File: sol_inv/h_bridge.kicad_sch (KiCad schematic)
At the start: 31 parts, among them J1 Screw_Terminal_01x02, J2 Screw_Terminal_01x02, T1 12uH, 1.7A, T2 12uH, 1.7A, T3 12uH, 1.7A, U1 MCP6001-OT, U2 MCP6001-OT, U3 INA240A1D, U4 INA240A1D, U5 IFX007T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

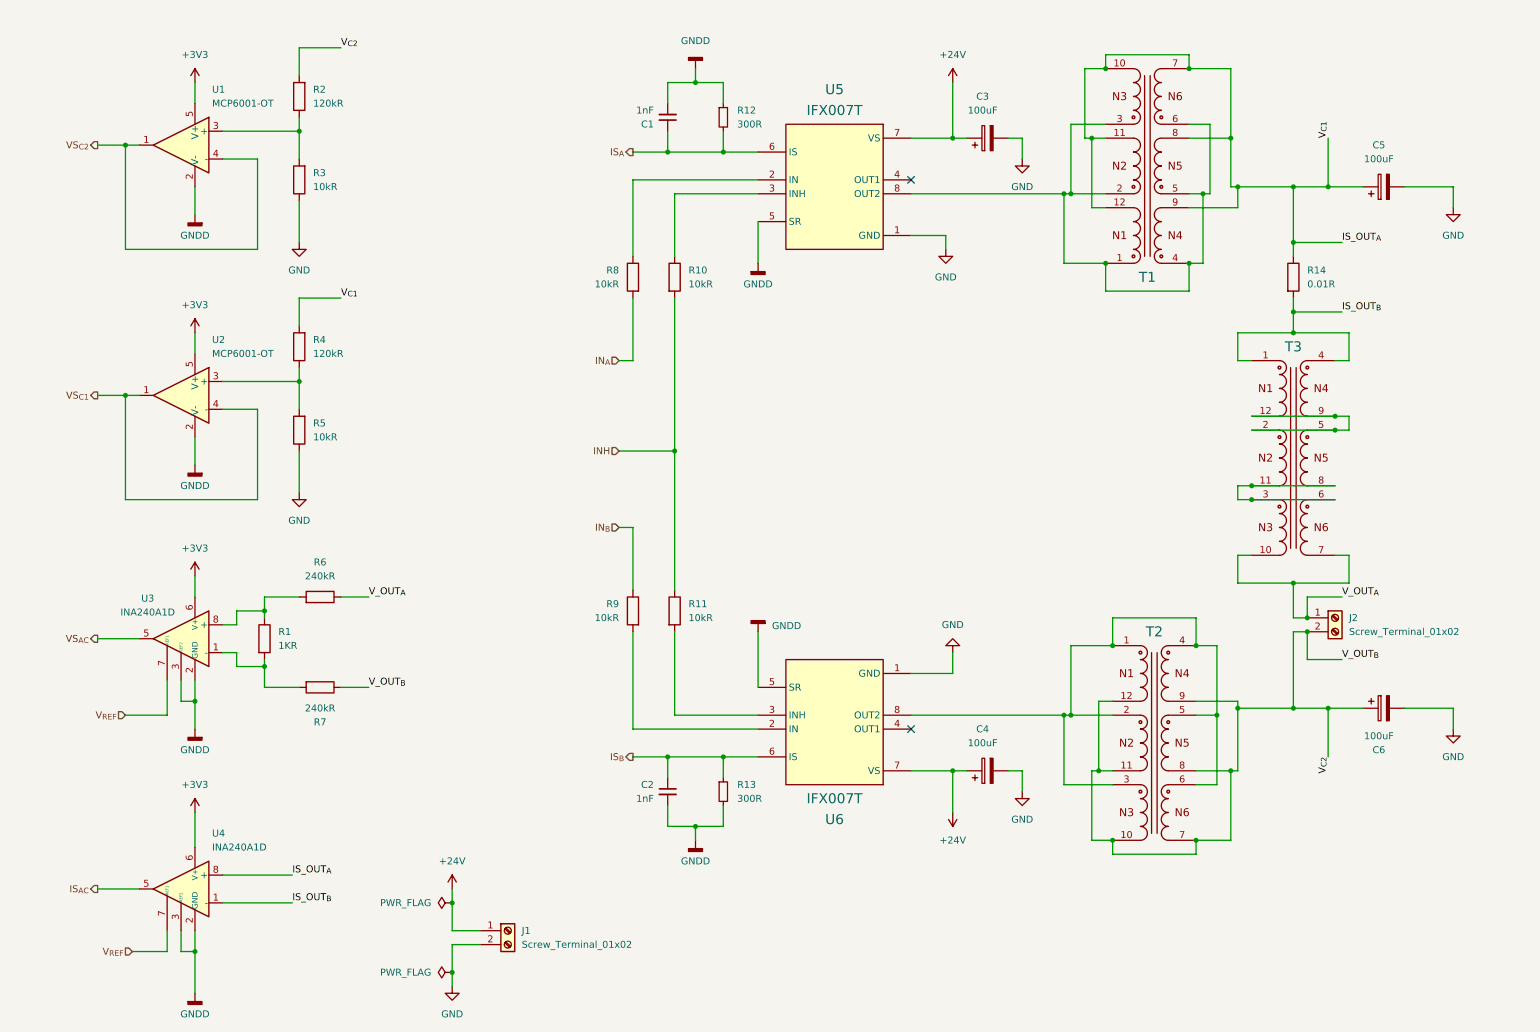
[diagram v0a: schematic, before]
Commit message: v0.2 components change + reference to providers
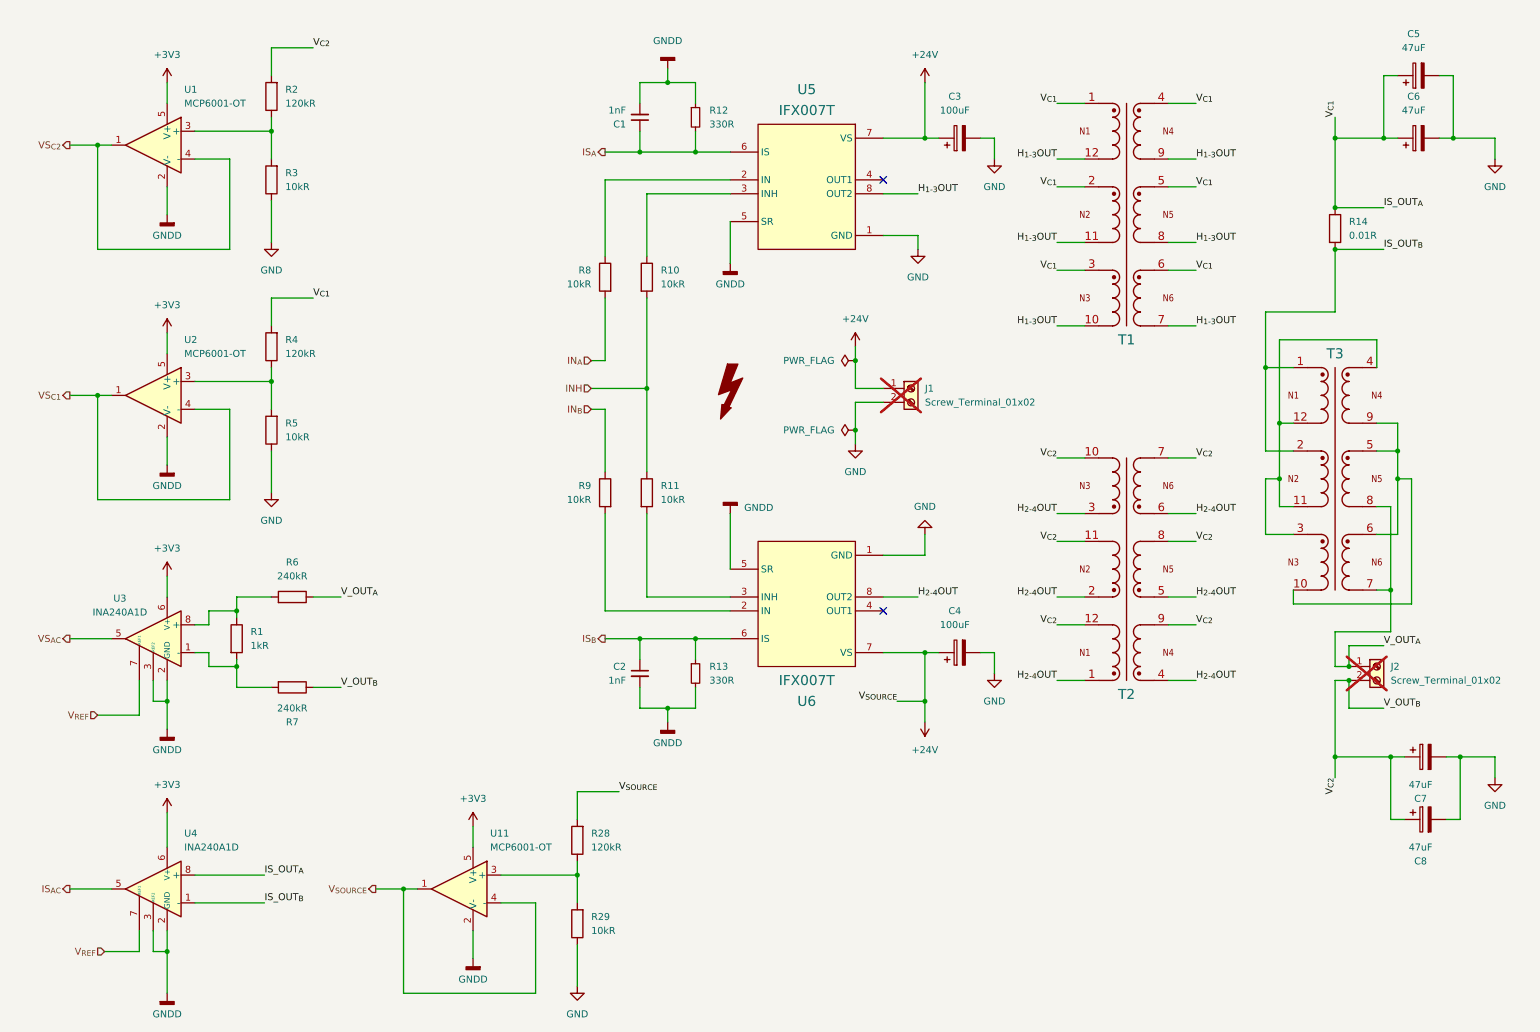
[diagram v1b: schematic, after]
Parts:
- removed C6: 100uF, Capacitor_SMD:CP_Elec_8x10, symbol Device:C_Polarized
- removed T3: 12uH, 1.7A, Eagle_WE-FLEX (rev24a):WE-FLEX_EFD20, symbol WE-FLEX (rev24a):749196521
- added C5, C7, C8: 47uF, Capacitor_SMD:CP_Elec_8x10, symbol Device:C_Polarized
- added R28: 120kR, Resistor_SMD:R_0805_2012Metric, symbol Device:R
- added R29: 10kR, Resistor_SMD:R_2512_6332Metric, symbol Device:R
- added T3: 12uH, 1.7A, Eagle_WE-FLEX (rev24a):WE-FLEX_EFD20, symbol Eagle_WE-FLEX (rev24a):WE-FLEX_EFD20
- added U11: MCP6001-OT, Package_TO_SOT_SMD:SOT-23-5, symbol Amplifier_Operational:MCP6001-OT
- C1, C2: ComponentLink2URL (none) -> https://ro.farnell.com/kemet/c0603c102k5recauto/cap-1000pf-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
- C3, C4: ComponentLink2URL (none) -> https://ro.farnell.com/nichicon/uud1h101mnl1gs/cap-100-f-50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
- C6: renamed from C5; value 100uF -> 47uF; ComponentLink2URL (none) -> https://ro.farnell.com/kemet/a785kn476m1jlas045/cap-alu-ele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
- J1, J2: footprint Wurth-691216610002:691216610002 -> Wurth-WR-TBL Series:691216610002_Handsolder; ComponentLink2URL (none) -> https://ro.farnell.com/wurth-elektronik/691216610002/tb-wir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; now not fitted; now left out of the parts list
- R1: value 1KR -> 1kR; ComponentLink2URL (none) -> https://ro.farnell.com/multicomp-pro/mcmr08x1001ftl/res-1k-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
- R10, R11, R3, R5, R8, R9: ComponentLink2URL (none) -> https://ro.farnell.com/vishay/crcw251210k0fkeg/res-10k-1-1w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
- R12, R13: value 300R -> 330R; footprint Resistor_SMD:R_0402_1005Metric -> Resistor_SMD:R_0603_1608Metric; ComponentLink2URL (none) -> https://ro.farnell.com/te-connectivity/crgcq0603j330r/res-3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
- R14: ComponentLink2URL (none) -> https://ro.farnell.com/te-connectivity/crgcq0603j330r/res-3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
- R2, R4: ComponentLink2URL (none) -> https://ro.farnell.com/panasonic/erjhp6j124v/res-120k-5-0-5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
- R6, R7: ComponentLink2URL (none) -> https://ro.farnell.com/panasonic/erj3red2403v/res-240k-0-5-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
- T1, T2: symbol WE-FLEX (rev24a):749196521 -> Eagle_WE-FLEX (rev24a):WE-FLEX_EFD20; ComponentLink1URL https://www.we-online.com/redexpert/article/749196521?ad -> (none); ComponentLink2URL https://www.we-online.com/redexpert/spec/749196521?ad -> https://ro.mouser.com/ProductDetail/Wurth-Elektronik/749196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
- U1, U2: ComponentLink2URL (none) -> https://ro.mouser.com/ProductDetail/Microchip-Technology/MC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
- U3, U4: ComponentLink2URL (none) -> https://ro.mouser.com/ProductDetail/Texas-Instruments/INA24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
- U5, U6: ComponentLink2URL (none) -> https://ro.mouser.com/ProductDetail/Infineon-Technologies/I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
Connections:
- net +24V: now also R28.2, U11.1, U11.4 (-)
- net +3V3: now also U11.5 (V+)
- net GND: now also C5.2, C7.2, C8.2, R29.1
- net GNDD: now also U11.2 (V-)
- net IS_OUT_{A}: now also T1.1, T1.2, T1.3, T1.4, T1.5, T1.6, C5.1; no longer T1.10, T1.11, T1.12, T1.7, T1.8, T1.9
- net IS_OUT_{B}: now also T3.1, T3.2
- net V_OUT_{A}: now also T3.7, T3.8
- net V_OUT_{B}: now also C7.1, C8.1
- net H_{2-4}OUT: now reaches T2.1, T2.2, T2.3, T2.4, T2.5, T2.6, U6.8 (OUT2)
- new net: R28.1, R29.2, U11.3 (+)
- new net: T3.10, T3.5, T3.6, T3.9
- new net: T3.11, T3.12, T3.3, T3.4
- new net H_{1-3}OUT: T1.10, T1.11, T1.12, T1.7, T1.8, T1.9, U5.8 (OUT2)
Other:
- moved on the sheet: C1, C2, C3, C4, C6, R1, R10, R11, R12, R13, R14, R2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

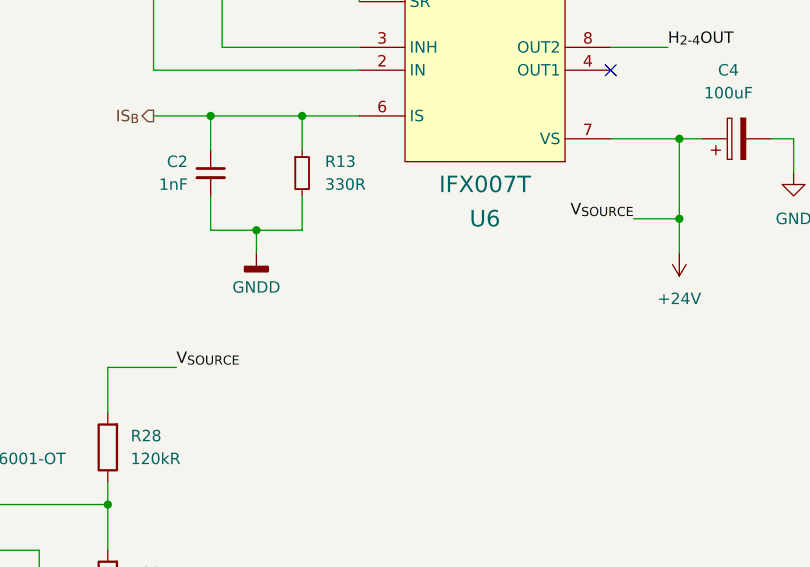
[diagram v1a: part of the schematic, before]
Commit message: initial component placement
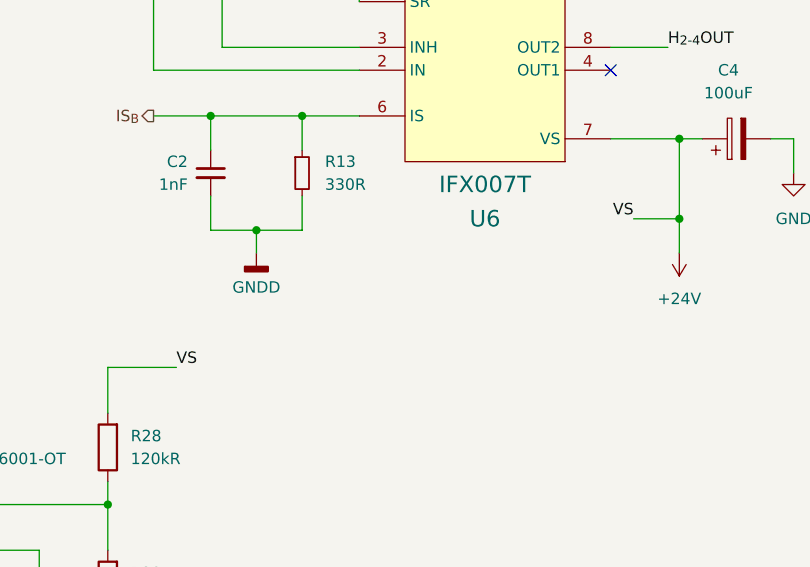
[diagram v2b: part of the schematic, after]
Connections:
- net +24V: no longer U11.1, U11.4 (-)
- new net V_{SOURCE}: U11.1, U11.4 (-)
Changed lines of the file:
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@@
 	(title_block
 		(title "H-Bridge Current Conversion")
-		(date "2025-04-10")
-		(rev "0.2")
+		(date "2025-04-24")
+		(rev "0.2.1")
 		(company "Cezar-Octavian Bontaș")
 	)
@@
 		)
 	)
-	(label "V_{SOURCE}"
+	(label "VS"
 		(at 171.45 135.89 180)
 		(effects
@@
 		)
 	)
-	(label "V_{SOURCE}"
+	(label "VS"
 		(at 120.65 152.4 0)
 		(effects
@@
 		(at 140.97 78.74 0)
 		(unit 1)
-		(exclude_from_sim yes)
+		(exclude_from_sim no)
 		(in_bom no)
 		(on_board no)

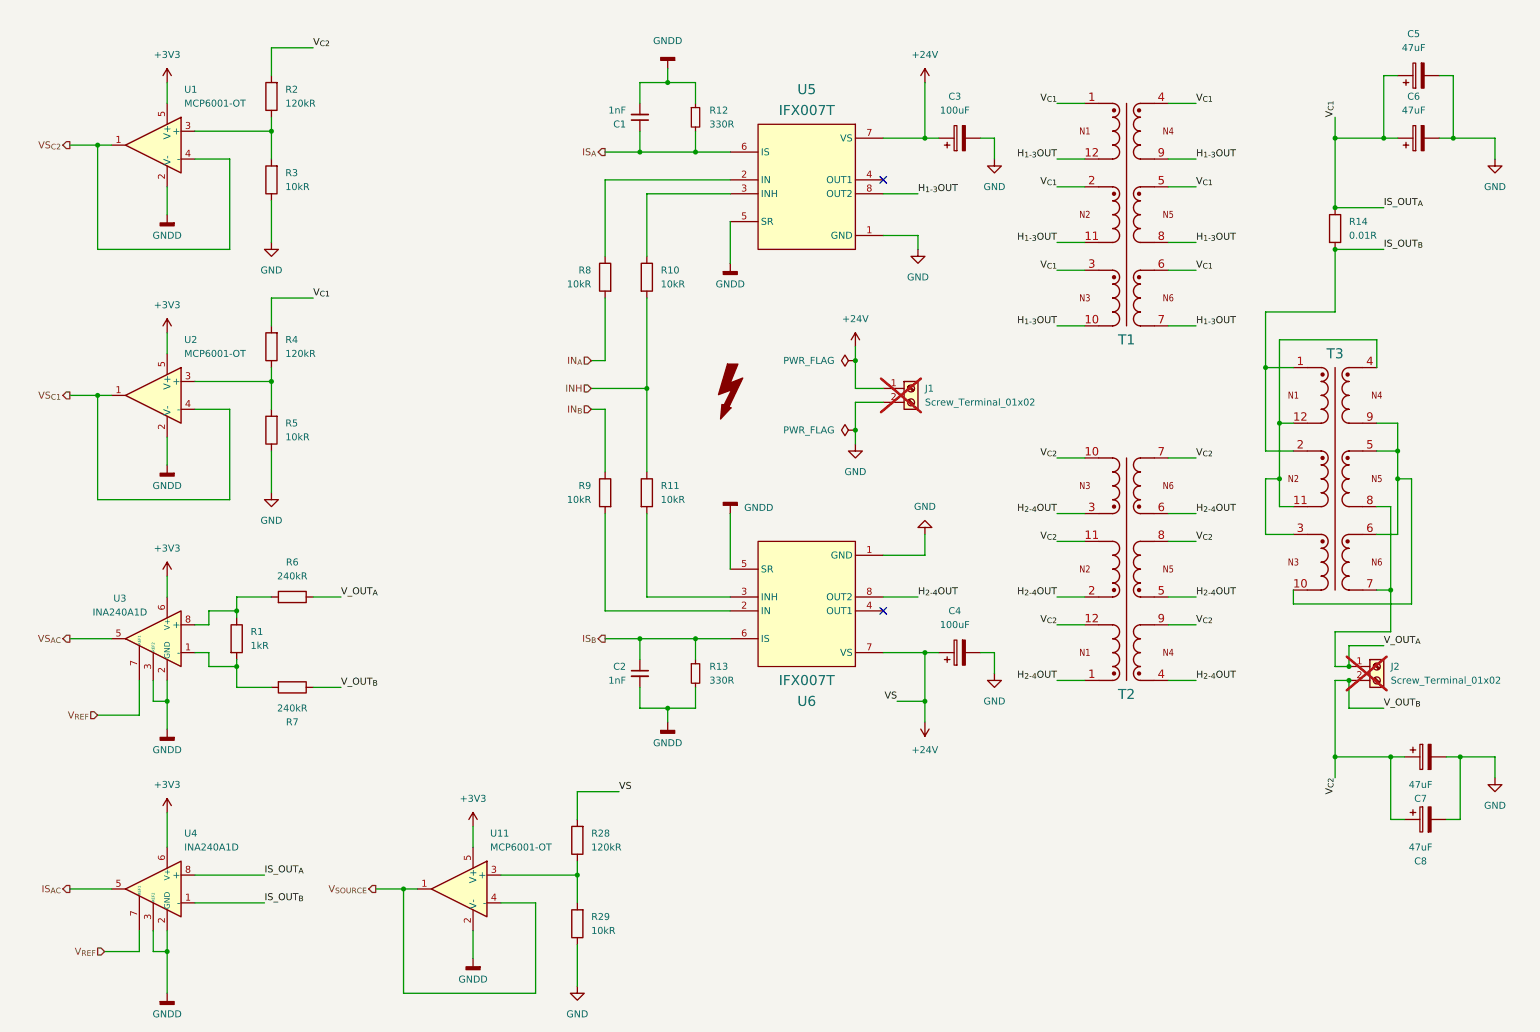
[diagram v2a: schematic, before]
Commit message: v0.3 pcb layout pre-drc fixes
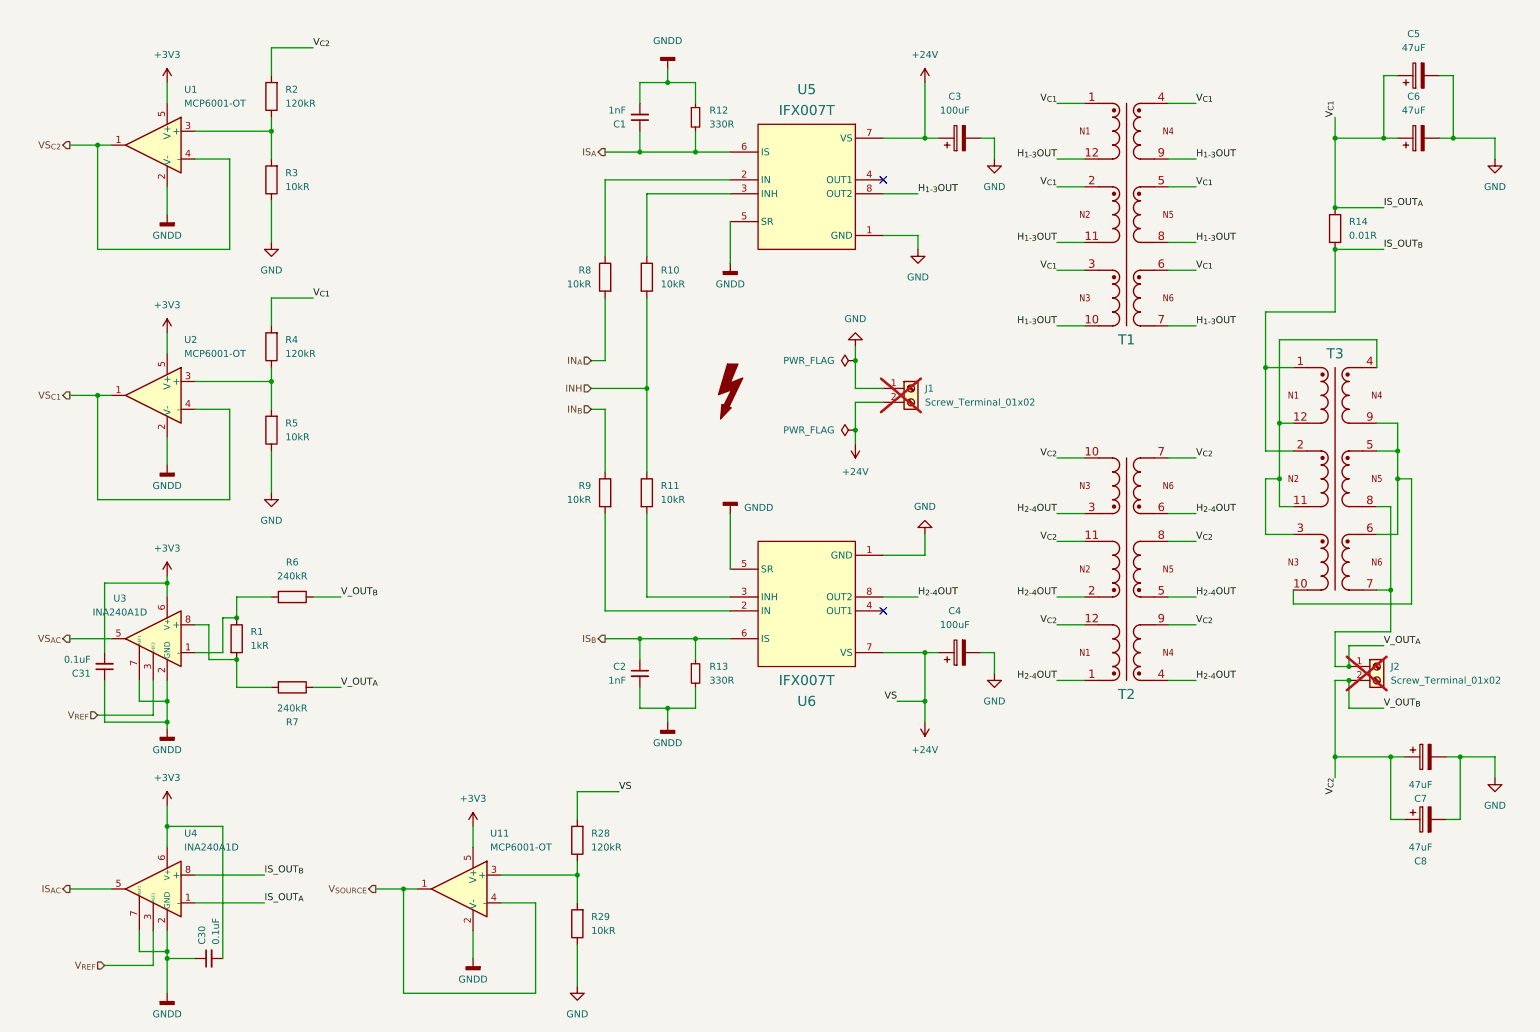
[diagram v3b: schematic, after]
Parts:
- added C30, C31: 0.1uF, Capacitor_SMD:C_0402_1005Metric, symbol Device:C_Small
- R10, R11, R29, R3, R5, R8, R9: footprint Resistor_SMD:R_2512_6332Metric -> Resistor_SMD:R_0402_1005Metric; ComponentLink2URL https://ro.farnell.com/vishay/crcw251210k0fkeg/res-10k-1-1w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 -> https://ro.farnell.com/multicomp-pro/mr04x1002ftlv/res-10k-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
- R14: footprint WSLP2512R0100FEA:RES_VISHAY_WSLP2512_C_VIS -> Resistor_SMD:R_2512_6332Metric
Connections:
- net +24V: now also J1.2 (Pin_2); no longer J1.1 (Pin_1)
- net +3V3: now also C30.2, C31.2
- net GND: now also J1.1 (Pin_1); no longer J1.2 (Pin_2)
- net GNDD: now also U3.7 (REF1), U4.7 (REF1), C30.1, C31.1; no longer U3.3 (REF2), U4.3 (REF2)
- net IS_OUT_{A}: now also U4.1 (-); no longer U4.8 (+)
- net IS_OUT_{B}: now also U4.8 (+); no longer U4.1 (-)
- net V_OUT_{A}: now also R7.1; no longer R6.1
- net V_OUT_{B}: now also R6.1; no longer R7.1
- net V_{REF}: now also U3.3 (REF2), U4.3 (REF2); no longer U3.7 (REF1), U4.7 (REF1)
- net at R1.2, R7.2: now also U3.8 (+); no longer U3.1 (-)
- net at R1.1, R6.2: now also U3.1 (-); no longer U3.8 (+)

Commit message: v0.3.1 drc fixes + layout tweaks
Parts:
- R14: ComponentLink2URL https://ro.farnell.com/te-connectivity/crgcq0603j330r/res-3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 -> https://ro.mouser.com/ProductDetail/Vishay-Dale/WSLP2512R01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
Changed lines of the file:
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@@
 	(title_block
 		(title "H-Bridge Current Conversion")
-		(date "2025-05-01")
-		(rev "0.3")
+		(date "2025-05-07")
+		(rev "0.3.1")
 		(company "Cezar-Octavian Bontaș")
 	)
@@
 			)
 		)
-		(property "ComponentLink2URL" "https://ro.farnell.com/te-connectivity/crgcq0603j330r/res-330r-5-0603-thick-film/dp/2861861"
+		(property "ComponentLink2URL" "https://ro.mouser.com/ProductDetail/Vishay-Dale/WSLP2512R0100FEA?qs=2spUtbtSOvj5wmRiEB0lew%3D%3D"
 			(at 251.46 49.53 0)
 			(effects
